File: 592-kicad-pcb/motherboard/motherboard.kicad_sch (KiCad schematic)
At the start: 1 part, among them U16 NUCLEO144-H743ZI

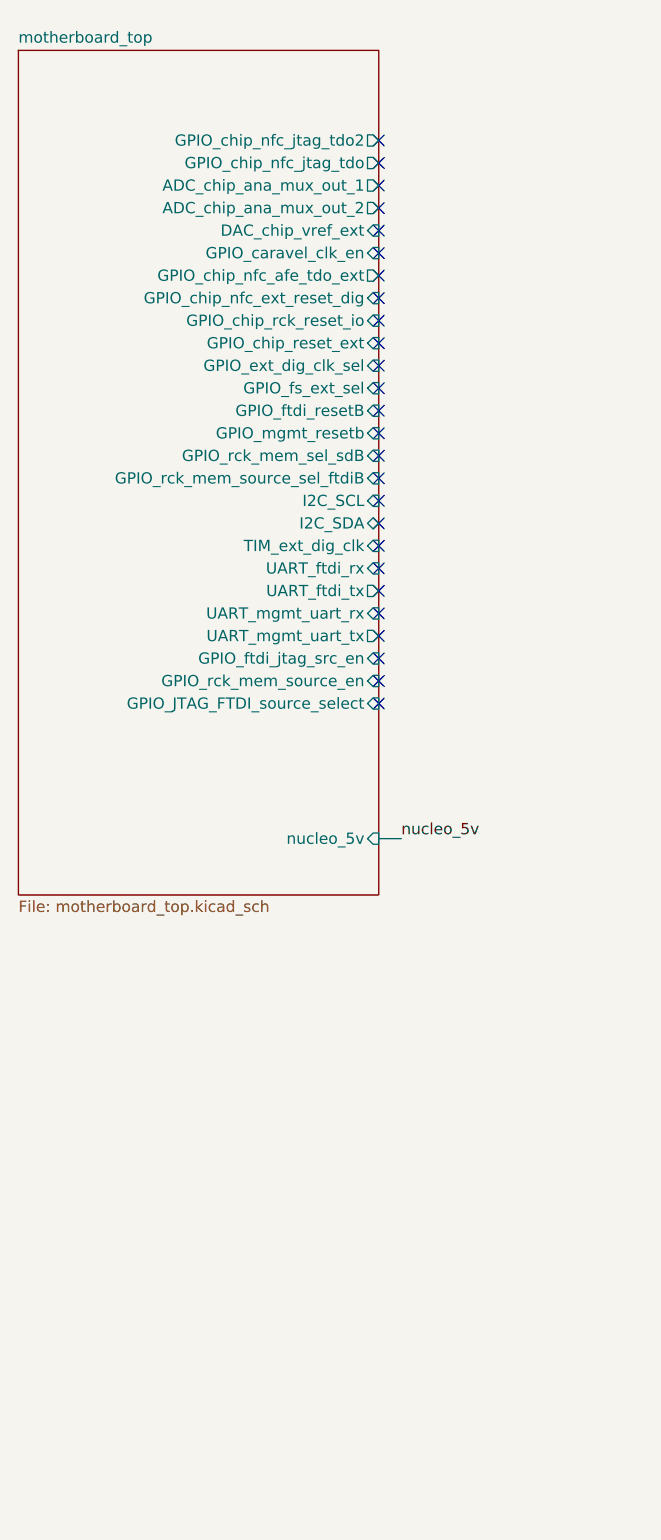
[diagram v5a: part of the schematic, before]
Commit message: add aux SPI dual-master to drive caravel CPU
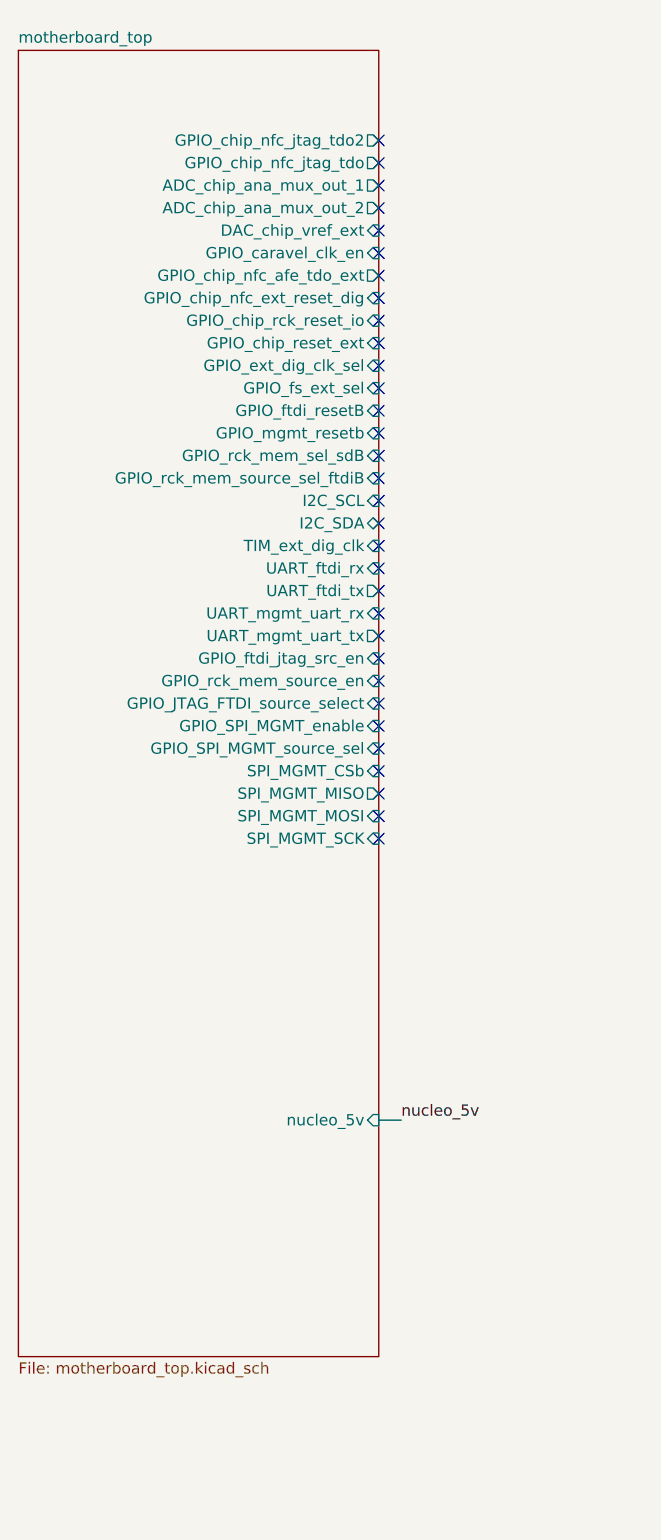
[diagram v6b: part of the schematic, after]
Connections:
- no-connect marks 38 -> 44
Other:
- sheet motherboard_top ports: added GPIO_SPI_MGMT_enable, GPIO_SPI_MGMT_source_sel, SPI_MGMT_CSb, SPI_MGMT_MISO, SPI_MGMT_MOSI, SPI_MGMT_SCK; removed none
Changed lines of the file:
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@@
+	)
+	(no_connect
+		(at 71.12 97.79)
 	)
 	(no_connect
@@
 	)
 	(no_connect
+		(at 71.12 100.33)
+	)
+	(no_connect
+		(at 71.12 95.25)
+	)
+	(no_connect
 		(at 71.12 31.75)
 	)
@@
 	)
 	(no_connect
+		(at 71.12 107.95)
+	)
+	(no_connect
 		(at 176.53 29.21)
 	)
@@
 	)
 	(no_connect
+		(at 71.12 102.87)
+	)
+	(no_connect
 		(at 123.19 80.01)
 	)
@@
 	)
 	(no_connect
+		(at 71.12 105.41)
+	)
+	(no_connect
 		(at 71.12 74.93)
 	)
@@
 	(wire
 		(pts
-			(xy 71.12 107.95) (xy 73.66 107.95)
+			(xy 71.12 139.7) (xy 73.66 139.7)
 		)
 		(stroke
@@
 	)
 	(label "nucleo_5v"
-		(at 73.66 107.95 0)
+		(at 73.66 139.7 0)
 		(effects
 			(font
@@
 	(sheet
 		(at 30.48 19.05)
-		(size 40.64 95.25)
+		(size 40.64 147.32)
 		(exclude_from_sim no)
 		(in_bom yes)
@@
 		)
 		(property "Sheetfile" "motherboard_top.kicad_sch"
-			(at 30.48 114.8846 0)
+			(at 30.48 166.9546 0)
 			(effects
 				(font
@@
 		)
 		(pin "nucleo_5v" input
-			(at 71.12 107.95 0)
+			(at 71.12 139.7 0)
 			(effects
 				(font
@@
 			(effects
 				(font
+					(size 1.27 1.27)
+				)
+				(justify right)
+			)
+		)
+		(pin "GPIO_SPI_MGMT_enable" input
+			(at 71.12 95.25 0)
+			(effects
+				(font
+					(size 1.27 1.27)
+				)
+				(justify right)
+			)
+		)
+		(pin "GPIO_SPI_MGMT_source_sel" input
+			(at 71.12 97.79 0)
+			(effects
+				(font
+					(size 1.27 1.27)
+				)
+				(justify right)
+			)
+		)
+		(pin "SPI_MGMT_CSb" input
+			(at 71.12 100.33 0)
+			(effects
+				(font
+					(size 1.27 1.27)
+				)
+				(justify right)
+			)
+		)
+		(pin "SPI_MGMT_MISO" output
+			(at 71.12 102.87 0)
+			(effects
+				(font
+					(size 1.27 1.27)
+				)
+				(justify right)
+			)
+		)
+		(pin "SPI_MGMT_MOSI" input
+			(at 71.12 105.41 0)
+			(effects
+				(font
+					(size 1.27 1.27)
+				)
+				(justify right)
+			)
+		)
+		(pin "SPI_MGMT_SCK" input
+			(at 71.12 107.95 0)
+			(effects
+				(font

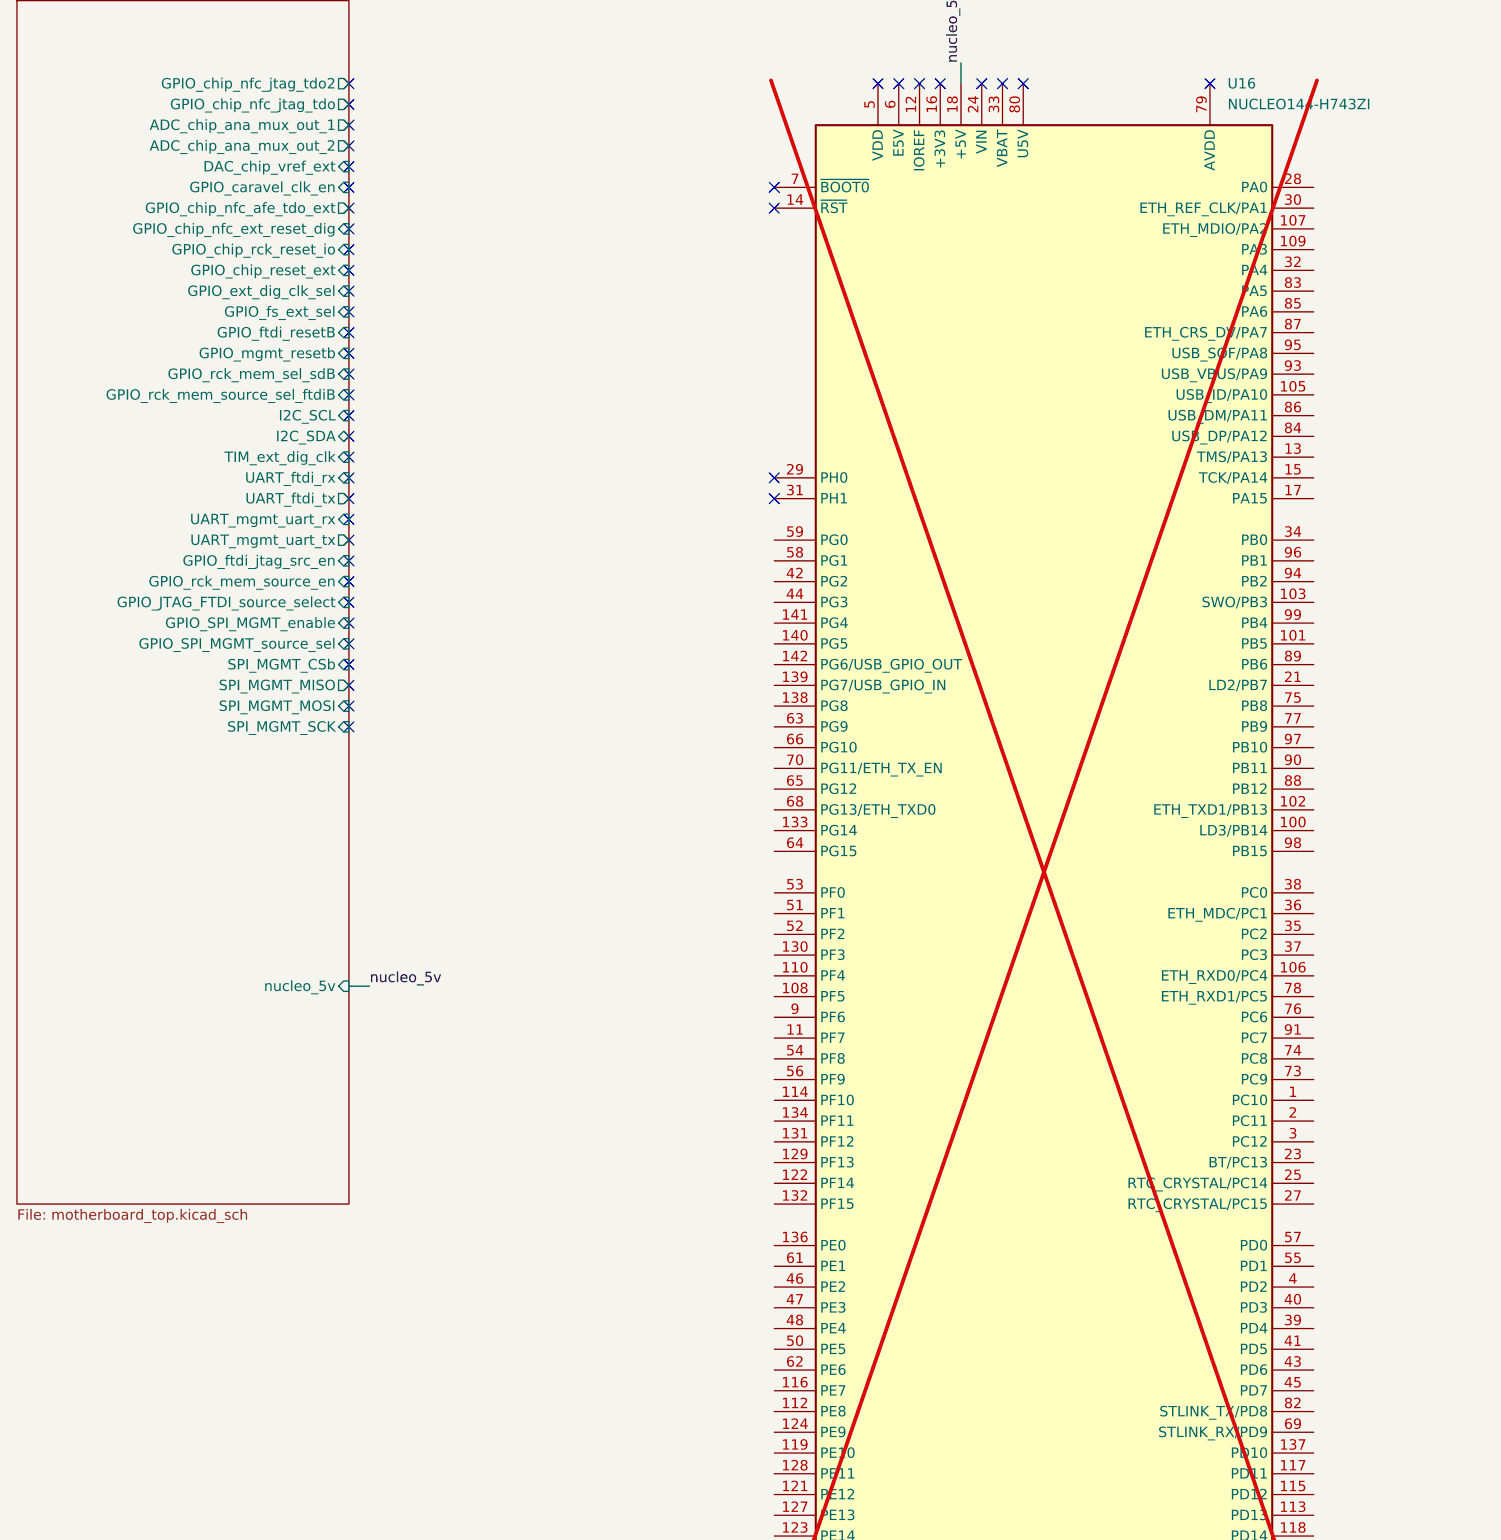
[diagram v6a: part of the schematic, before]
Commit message: map to STM pins
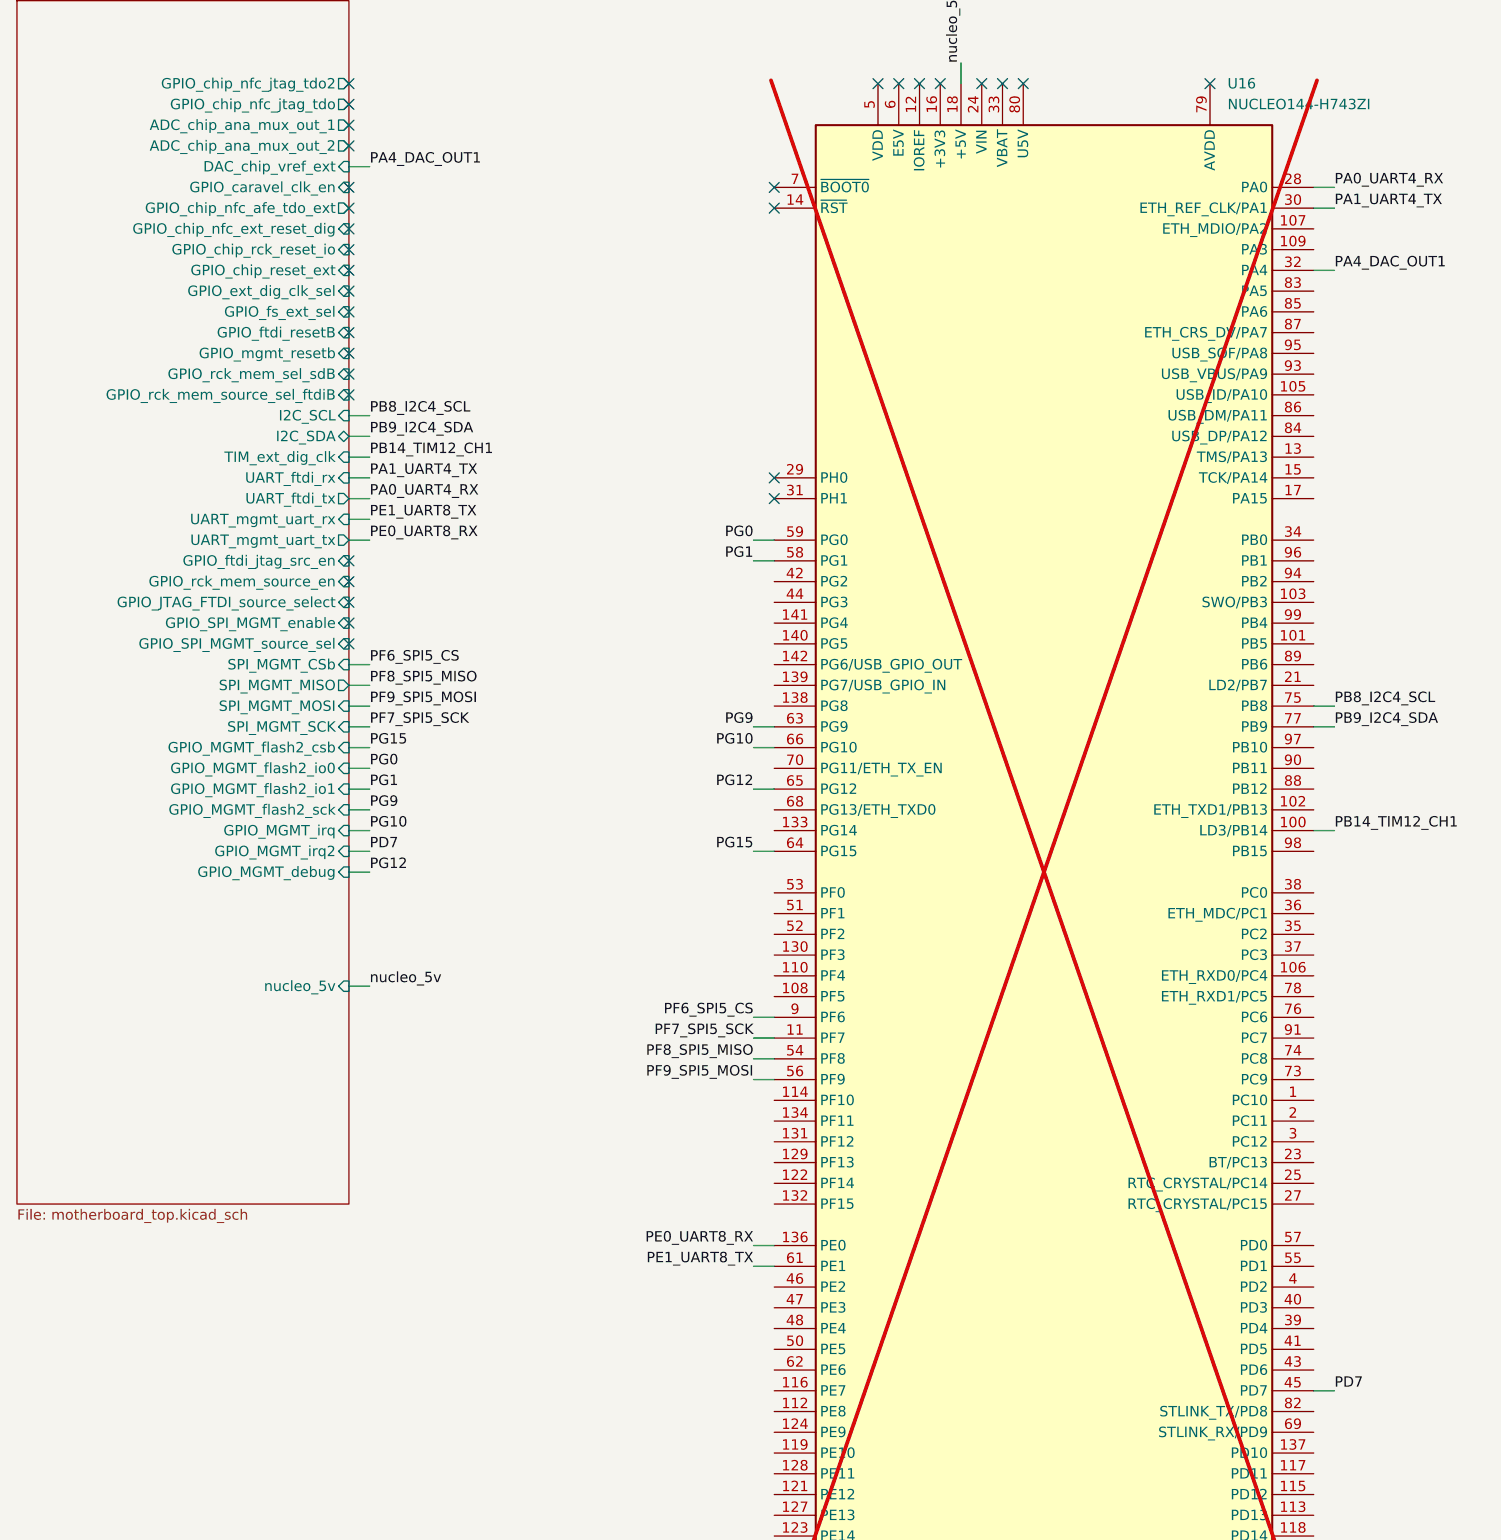
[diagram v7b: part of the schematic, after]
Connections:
- net PB14_TIM12_CH1: now reaches U16.100 (LD3/PB14)
- net PF7_SPI5_SCK: now reaches U16.11 (PF7)
- net PE0_UART8_RX: now reaches U16.136 (PE0)
- net PA0_UART4_RX: now reaches U16.28 (PA0)
- net PA1_UART4_TX: now reaches U16.30 (ETH_REF_CLK/PA1)
- net PA4_DAC_OUT1: now reaches U16.32 (PA4)
- net PD7: now reaches U16.45 (PD7)
- net PF8_SPI5_MISO: now reaches U16.54 (PF8)
- net PF9_SPI5_MOSI: now reaches U16.56 (PF9)
- net PG1: now reaches U16.58 (PG1)
- net PG0: now reaches U16.59 (PG0)
- net PE1_UART8_TX: now reaches U16.61 (PE1)
- net PG9: now reaches U16.63 (PG9)
- net PG15: now reaches U16.64 (PG15)
- net PG12: now reaches U16.65 (PG12)
- net PG10: now reaches U16.66 (PG10)
- net PB8_I2C4_SCL: now reaches U16.75 (PB8)
- net PB9_I2C4_SDA: now reaches U16.77 (PB9)
- net PF6_SPI5_CS: now reaches U16.9 (PF6)
- no-connect marks 44 -> 32
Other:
- sheet motherboard_top ports: added GPIO_MGMT_debug, GPIO_MGMT_flash2_csb, GPIO_MGMT_flash2_io0, GPIO_MGMT_flash2_io1, GPIO_MGMT_flash2_sck, GPIO_MGMT_irq, GPIO_MGMT_irq2; removed none

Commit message: updates to routing
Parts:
- renumbered U16 to U1
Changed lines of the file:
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@@
 		(dnp yes)
 		(fields_autoplaced yes)
-		(property "Reference" "U16"
+		(property "Reference" "U1"
 			(at 178.6733 29.21 0)
 			(effects
@@
 			(project ""
 				(path "/5b0c97ac-fa03-4db8-b41b-0eee32b6f55d"
-					(reference "U16")
+					(reference "U1")
 					(unit 1)
 				)
@@
 		(dnp no)
 		(fields_autoplaced yes)
-		(property "Reference" "#PWR0157"
+		(property "Reference" "#PWR01"
 			(at 135.89 233.68 0)
 			(effects
@@
 			(project ""
 				(path "/5b0c97ac-fa03-4db8-b41b-0eee32b6f55d"
-					(reference "#PWR0157")
+					(reference "#PWR01")
 					(unit 1)
 				)
